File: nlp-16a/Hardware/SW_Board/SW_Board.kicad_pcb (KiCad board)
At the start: 2 copper layers, 70.5 x 40 mm, 10 parts, among them J1 Conn_02x10_Odd_Even, J2 Conn_02x10_Odd_Even, J3 USB-PWR, J4 Screw_Terminal_01x02, J5 Screw_Terminal_01x02, SW1 SW_DIP_x04, SW2 SW_DIP_x08

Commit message: 見積もり他
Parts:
- moved J4 12.7 mm to (113.0, 66.7)
- moved J5 12.7 mm to (113.0, 79.4)
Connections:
- J1 pad 1: DATA0 -> unconnected-(J1-Pad1)
- J1 pad 10: unconnected-(J1-Pad10) -> DATA2
- J1 pad 11: DATA5 -> unconnected-(J1-Pad11)
- J1 pad 12: unconnected-(J1-Pad12) -> DATA3
- J1 pad 13: DATA6 -> unconnected-(J1-Pad13)
- J1 pad 14: unconnected-(J1-Pad14) -> DATA4
- J1 pad 15: DATA7 -> DATA10
- J1 pad 16: unconnected-(J1-Pad16) -> DATA5
- J1 pad 17: VCC -> DATA9
- J1 pad 18: unconnected-(J1-Pad18) -> DATA6
- J1 pad 19: unconnected-(J1-Pad19) -> DATA8
- J1 pad 2: DATA8 -> unconnected-(J1-Pad2)
- J1 pad 20: unconnected-(J1-Pad20) -> DATA7
- J1 pad 3: DATA1 -> unconnected-(J1-Pad3)
- J1 pad 4: DATA9 -> VCC
- J1 pad 5: DATA2 -> unconnected-(J1-Pad5)
- J1 pad 6: DATA10 -> DATA0
- J1 pad 7: DATA3 -> unconnected-(J1-Pad7)
- J1 pad 8: unconnected-(J1-Pad8) -> DATA1
- J1 pad 9: DATA4 -> unconnected-(J1-Pad9)
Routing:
- net DATA8: track 64.9 -> 37.6 mm
- net DATA9: track 68.3 -> 46.1 mm
- net DATA10: track 72.2 -> 52.5 mm
- net DATA6: track 58.3 -> 48.0 mm
- net DATA3: track 77.3 -> 67.1 mm
- net DATA7: track 51.9 -> 41.7 mm
- net DATA4: track 71.0 -> 60.7 mm
- net DATA2: track 83.7 -> 73.4 mm
- net DATA5: track 64.6 -> 55.0 mm
- net VCC: track 139.7 -> 130.1 mm
- net DATA0: track 84.4 -> 86.1 mm, vias 1 -> 0
- net DATA1: track 78.7 -> 79.8 mm, vias 1 -> 0

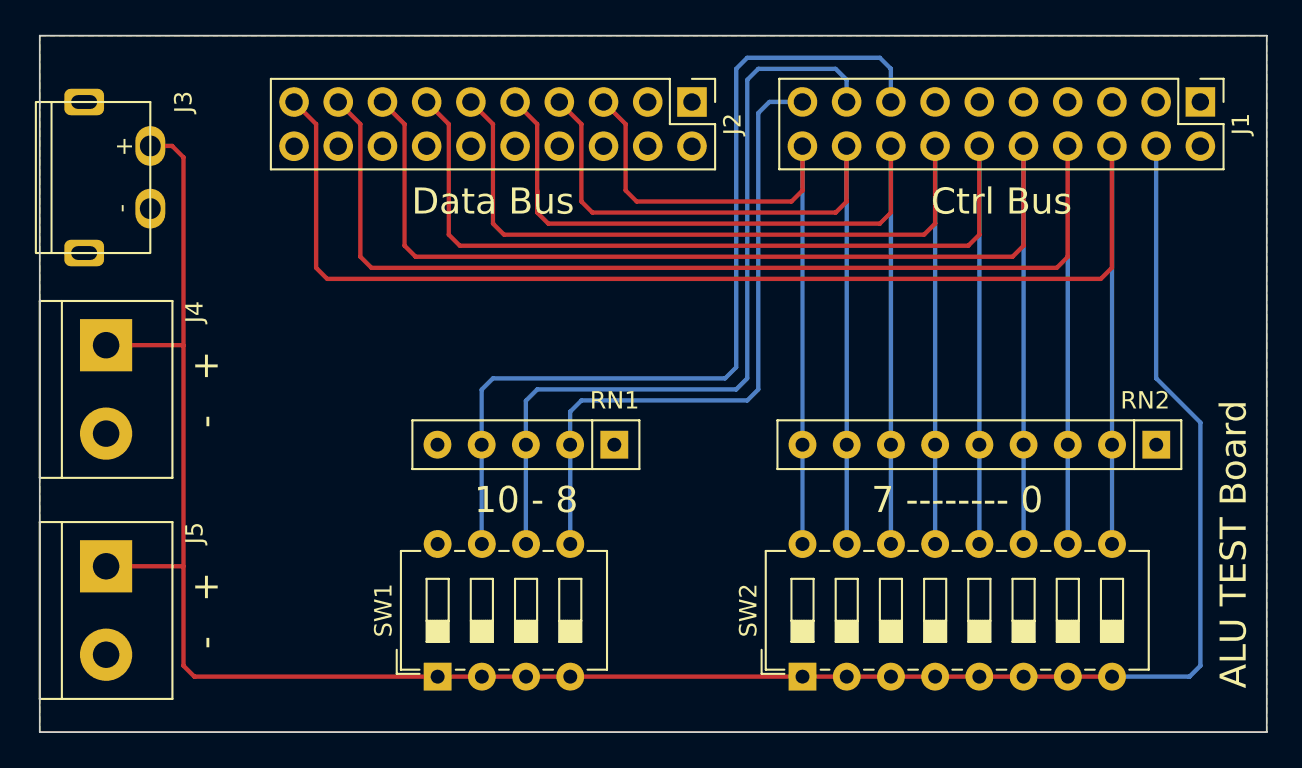
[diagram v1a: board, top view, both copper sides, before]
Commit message: ALU手動テストボード使いやすいように更新
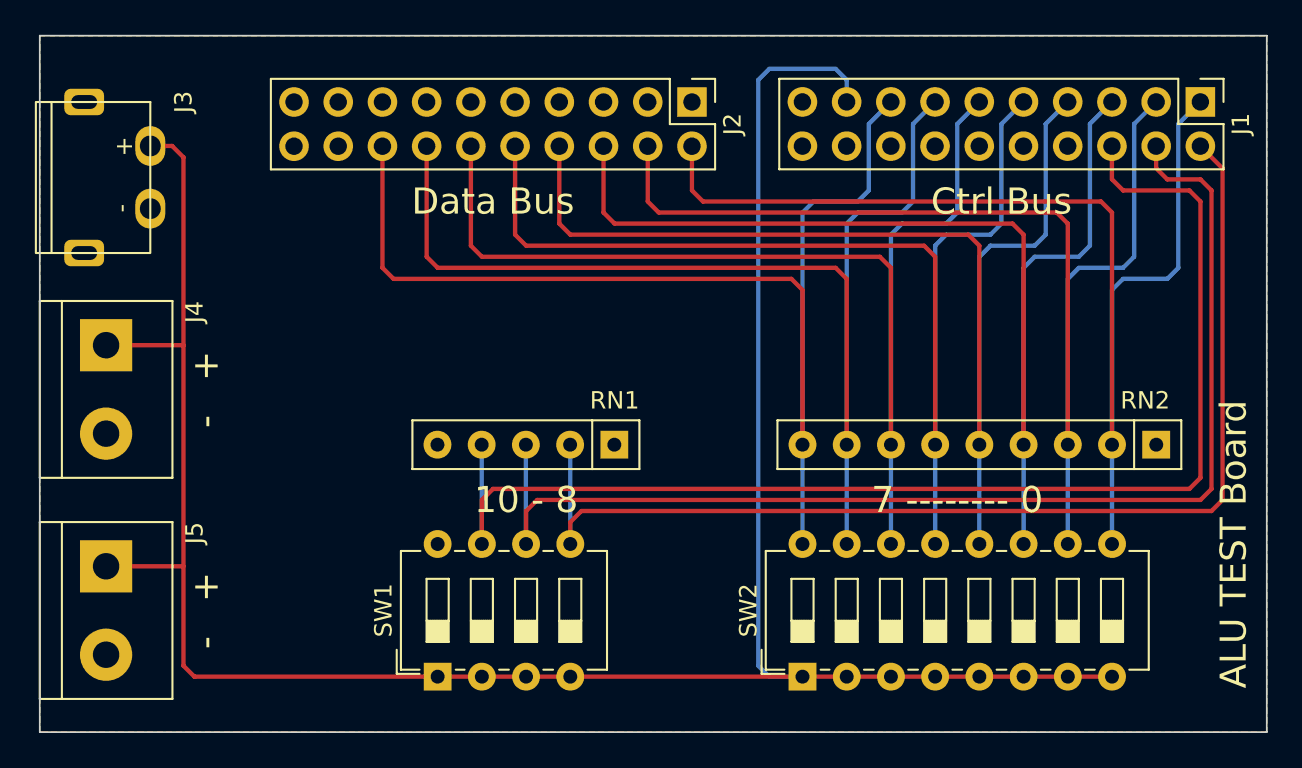
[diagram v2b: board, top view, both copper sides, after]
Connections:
- J1 pad 1: unconnected-(J1-Pad1) -> DATA0
- J1 pad 10: DATA2 -> unconnected-(J1-Pad10)
- J1 pad 11: unconnected-(J1-Pad11) -> DATA5
- J1 pad 12: DATA3 -> unconnected-(J1-Pad12)
- J1 pad 13: unconnected-(J1-Pad13) -> DATA6
- J1 pad 14: DATA4 -> unconnected-(J1-Pad14)
- J1 pad 15: DATA10 -> DATA7
- J1 pad 16: DATA5 -> unconnected-(J1-Pad16)
- J1 pad 17: DATA9 -> VCC
- J1 pad 18: DATA6 -> unconnected-(J1-Pad18)
- J1 pad 19: DATA8 -> unconnected-(J1-Pad19)
- J1 pad 2: unconnected-(J1-Pad2) -> DATA8
- J1 pad 20: DATA7 -> unconnected-(J1-Pad20)
- J1 pad 3: unconnected-(J1-Pad3) -> DATA1
- J1 pad 4: VCC -> DATA9
- J1 pad 5: unconnected-(J1-Pad5) -> DATA2
- J1 pad 6: DATA0 -> DATA10
- J1 pad 7: unconnected-(J1-Pad7) -> DATA3
- J1 pad 8: DATA1 -> unconnected-(J1-Pad8)
- J1 pad 9: unconnected-(J1-Pad9) -> DATA4
- J2 pad 10: unconnected-(J2-Pad10) -> DATA4
- J2 pad 11: DATA4 -> unconnected-(J2-Pad11)
- J2 pad 12: unconnected-(J2-Pad12) -> DATA5
- J2 pad 13: DATA3 -> unconnected-(J2-Pad13)
- J2 pad 14: unconnected-(J2-Pad14) -> DATA6
- J2 pad 15: DATA2 -> unconnected-(J2-Pad15)
- J2 pad 16: unconnected-(J2-Pad16) -> DATA7
- J2 pad 17: DATA1 -> unconnected-(J2-Pad17)
- J2 pad 19: DATA0 -> unconnected-(J2-Pad19)
- J2 pad 2: unconnected-(J2-Pad2) -> DATA0
- J2 pad 4: unconnected-(J2-Pad4) -> DATA1
- J2 pad 5: DATA7 -> unconnected-(J2-Pad5)
- J2 pad 6: unconnected-(J2-Pad6) -> DATA2
- J2 pad 7: DATA6 -> unconnected-(J2-Pad7)
- J2 pad 8: unconnected-(J2-Pad8) -> DATA3
- J2 pad 9: DATA5 -> unconnected-(J2-Pad9)
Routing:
- net DATA8: track 37.6 -> 65.8 mm
- net DATA7: track 41.7 -> 69.5 mm
- net DATA9: track 46.1 -> 69.6 mm
- net DATA6: track 48.0 -> 69.5 mm
- net DATA10: track 52.5 -> 73.4 mm
- net DATA0: track 86.1 -> 69.5 mm
- net DATA5: track 55.0 -> 69.5 mm
- net DATA1: track 79.8 -> 69.5 mm
- net DATA4: track 60.7 -> 69.5 mm
- net VCC: track 130.1 -> 137.2 mm
- net DATA2: track 73.4 -> 69.5 mm
- net DATA3: track 67.1 -> 69.5 mm
